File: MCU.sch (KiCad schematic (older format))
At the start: 37 parts, among them SW1 SW_Push, U1 STM32F407IGTx, Y1 12MHz, 20pF

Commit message: small revisions
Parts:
- added F?: 500mA, symbol Device:Fuse
- added J?: USB_B_Mini, symbol Connector:USB_B_Mini
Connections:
- net GND: now also J?.5 (GND), J?.6 (Shield)
- new net: F?.2, J?.1 (VBUS)
- new net 5V_USB: F?.1
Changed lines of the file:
@@
 U 1 1 5FAB40A6
 P 5500 1350
-F 0 "R2" V 5295 1350 50  0000 C CNN
-F 1 "1k" V 5386 1350 50  0000 C CNN
+F 0 "R2" V 5450 1250 50  0000 C CNN
+F 1 "1k" V 5450 1450 50  0000 C CNN
 F 2 "" H 5500 1350 50  0001 C CNN
 F 3 "~" H 5500 1350 50  0001 C CNN
@@
 U 1 1 5FAECA97
 P 6050 2150
-F 0 "R4" V 5845 2150 50  0000 C CNN
-F 1 "1k" V 5936 2150 50  0000 C CNN
+F 0 "R4" V 6100 2250 50  0000 C CNN
+F 1 "1k" V 6100 2050 50  0000 C CNN
 F 2 "" H 6050 2150 50  0001 C CNN
 F 3 "~" H 6050 2150 50  0001 C CNN
@@
 U 1 1 5FAF53A2
 P 6050 1750
-F 0 "R3" V 5845 1750 50  0000 C CNN
-F 1 "10k" V 5936 1750 50  0000 C CNN
+F 0 "R3" V 6000 1650 50  0000 C CNN
+F 1 "10k" V 6000 1850 50  0000 C CNN
 F 2 "" H 6050 1750 50  0001 C CNN
 F 3 "~" H 6050 1750 50  0001 C CNN
@@
 	12700 2400 12700 2600
 Connection ~ 12700 2600
+$Comp
+L Connector:USB_B_Mini J?
+U 1 1 5FA69DAF
+P 1750 2850
+F 0 "J?" H 1807 3317 50  0000 C CNN
+F 1 "USB_B_Mini" H 1807 3226 50  0000 C CNN
+F 2 "" H 1900 2800 50  0001 C CNN
+F 3 "~" H 1900 2800 50  0001 C CNN
+	1    1750 2850
+	1    0    0    -1
+$EndComp
+Text GLabel 2550 2400 1    50   Input ~ 0
+5V_USB
+$Comp
+L Device:Fuse F?
+U 1 1 5FA6B443
+P 2300 2650
+F 0 "F?" V 2103 2650 50  0000 C CNN
+F 1 "500mA" V 2194 2650 50  0000 C CNN
+F 2 "" V 2230 2650 50  0001 C CNN
+F 3 "~" H 2300 2650 50  0001 C CNN
+	1    2300 2650
+	0    1    1    0
+$EndComp
+Wire Wire Line
+	2550 2400 2550 2650
+Wire Wire Line
+	2550 2650 2450 2650
+Wire Wire Line
+	2150 2650 2050 2650
+Wire Wire Line
+	1750 3250 1750 3400
+Wire Wire Line
+	1750 3400 1650 3400
+Wire Wire Line
+	1650 3400 1650 3250
+$Comp
+L power:GND #PWR?
+U 1 1 5FA8CDC1
+P 1650 3550
+F 0 "#PWR?" H 1650 3300 50  0001 C CNN
+F 1 "GND" H 1655 3377 50  0000 C CNN
+F 2 "" H 1650 3550 50  0001 C CNN
+F 3 "" H 1650 3550 50  0001 C CNN
+	1    1650 3550
+	1    0    0    -1
+$EndComp
+Wire Wire Line
+	1650 3550 1650 3400
+Connection ~ 1650 3400
 $EndSCHEMATC

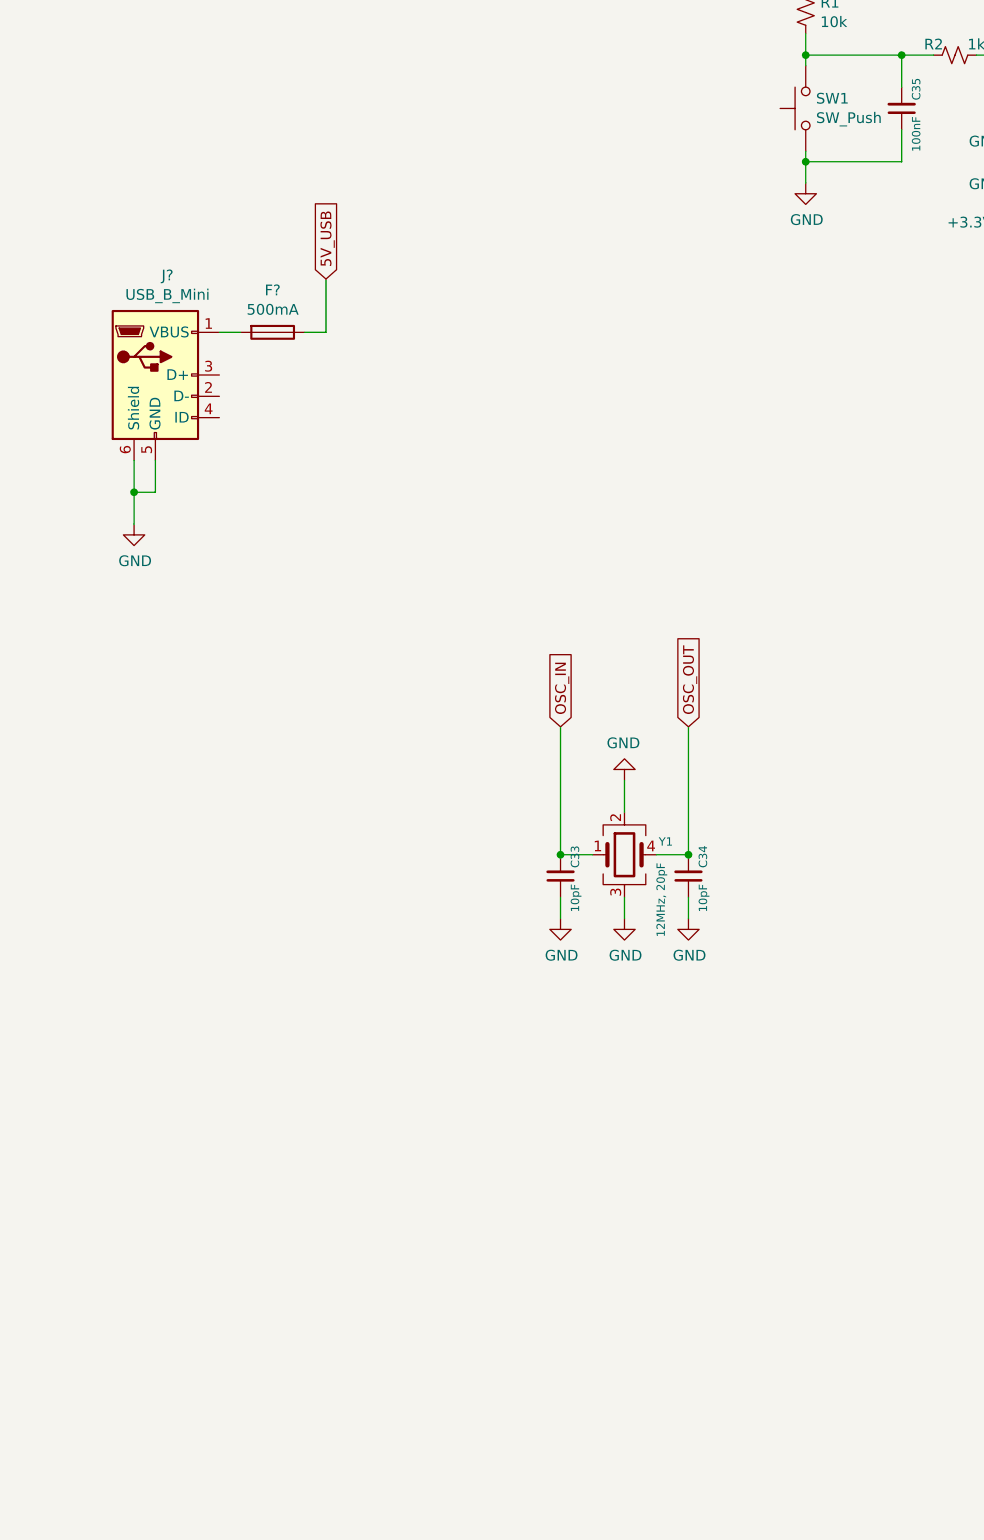
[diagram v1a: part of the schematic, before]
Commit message: added USB and micro SD card
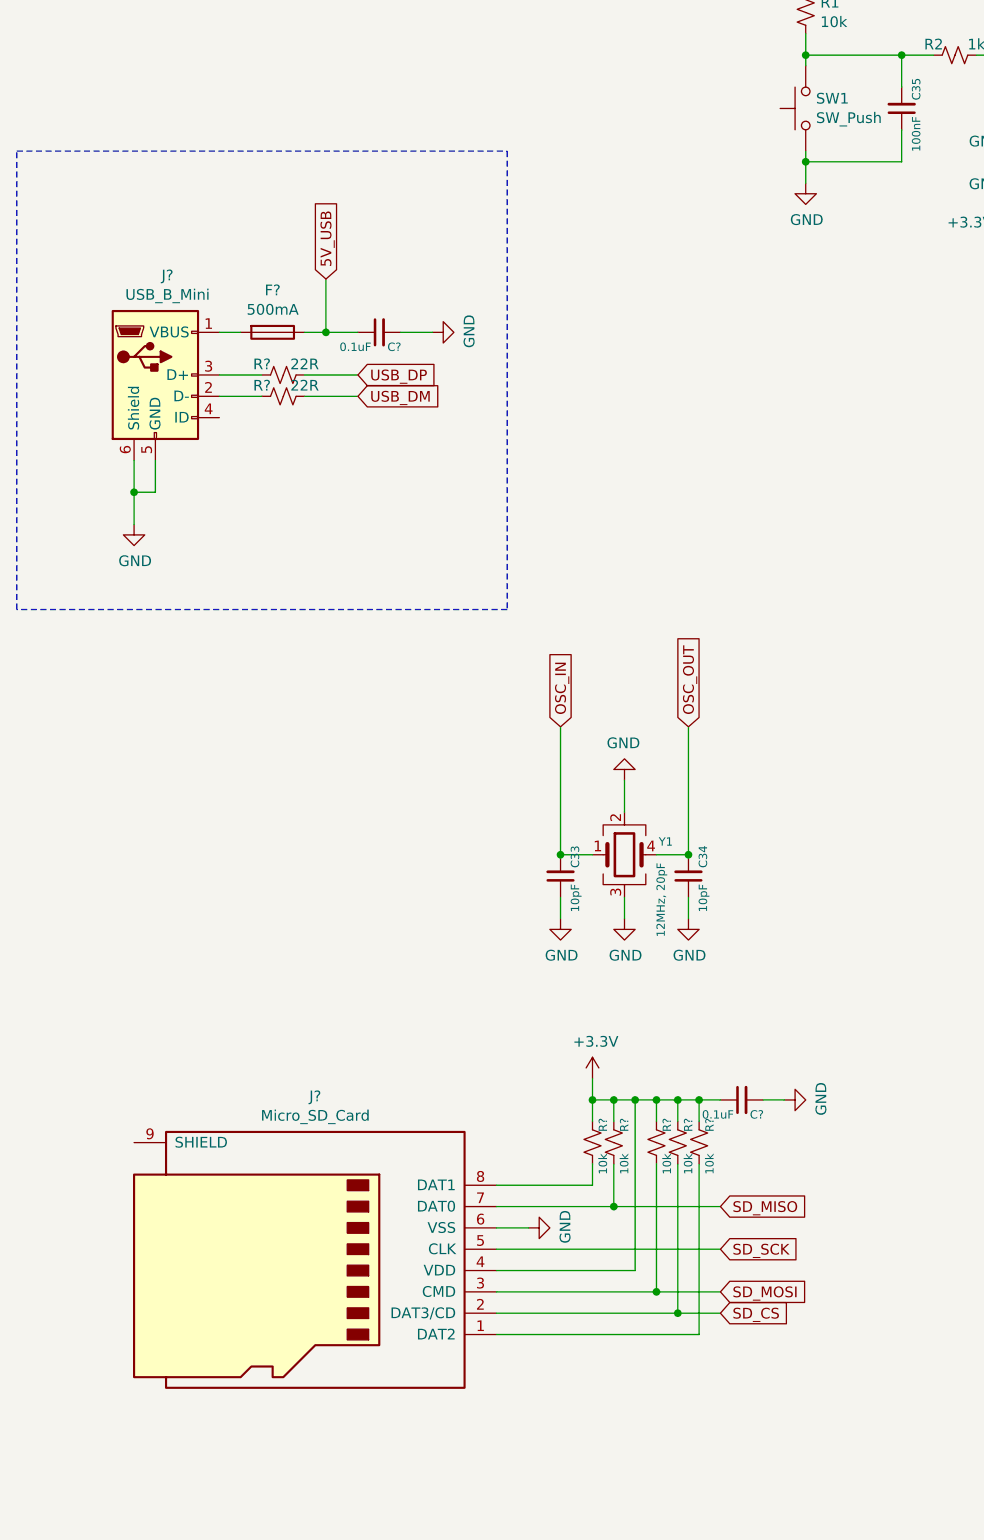
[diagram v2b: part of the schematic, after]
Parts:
- added C? (x2): 0.1uF, symbol Device:C_Small
- added J?: Micro_SD_Card, symbol Connector:Micro_SD_Card
- added R? (x2): 22R, symbol Device:R_Small_US
- added R? (x5): 10k, symbol Device:R_Small_US
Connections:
- net +3V3: now also C?.1, J?.4 (VDD), R?.1, R?.1, R?.1, R?.1, R?.1
- net 5V_USB: now also C?.1
- net GND: now also C?.2, C?.2, J?.6 (VSS)
- net at J?.2 (D-): now also R?.2
- net at J?.3 (D+): now also R?.2
- new net: J?.1 (DAT2), R?.2
- new net: J?.8 (DAT1), R?.2
- new net SD_CS: J?.2 (DAT3/CD), R?.2
- new net SD_MISO: J?.7 (DAT0), R?.2
- new net SD_MOSI: J?.3 (CMD), R?.2
- new net SD_SCK: J?.5 (CLK)
- new net USB_DM: R?.1
- new net USB_DP: R?.1

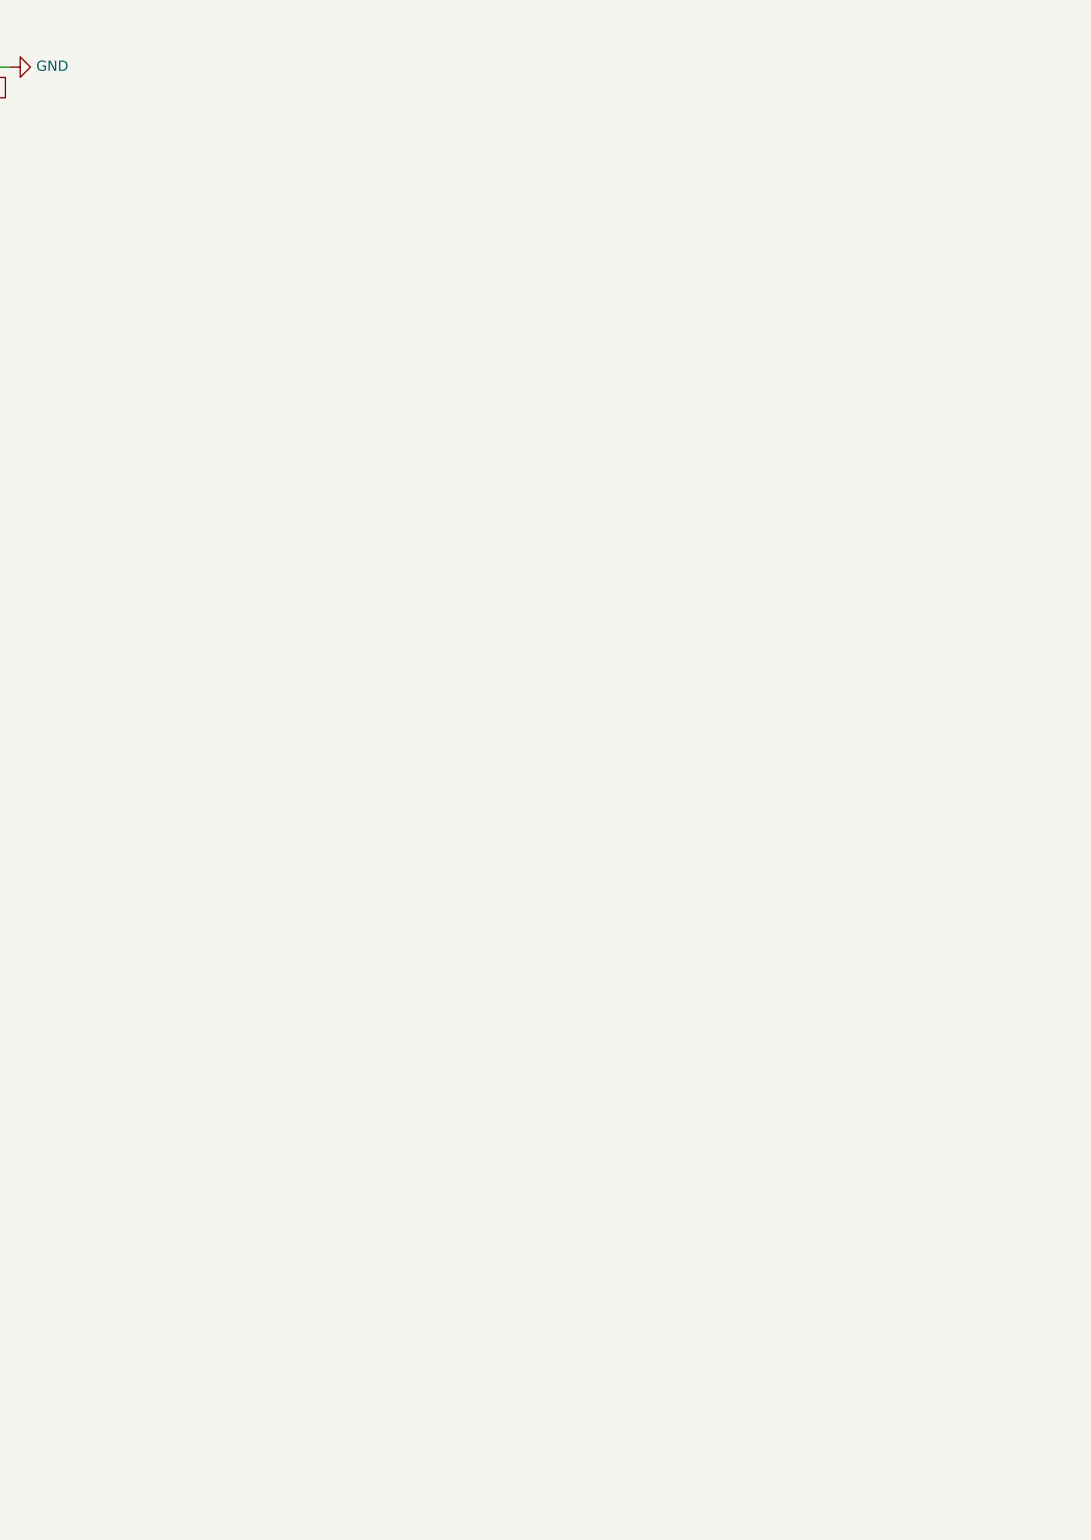
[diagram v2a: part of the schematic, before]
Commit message: added EEPROM and peripheral libraries
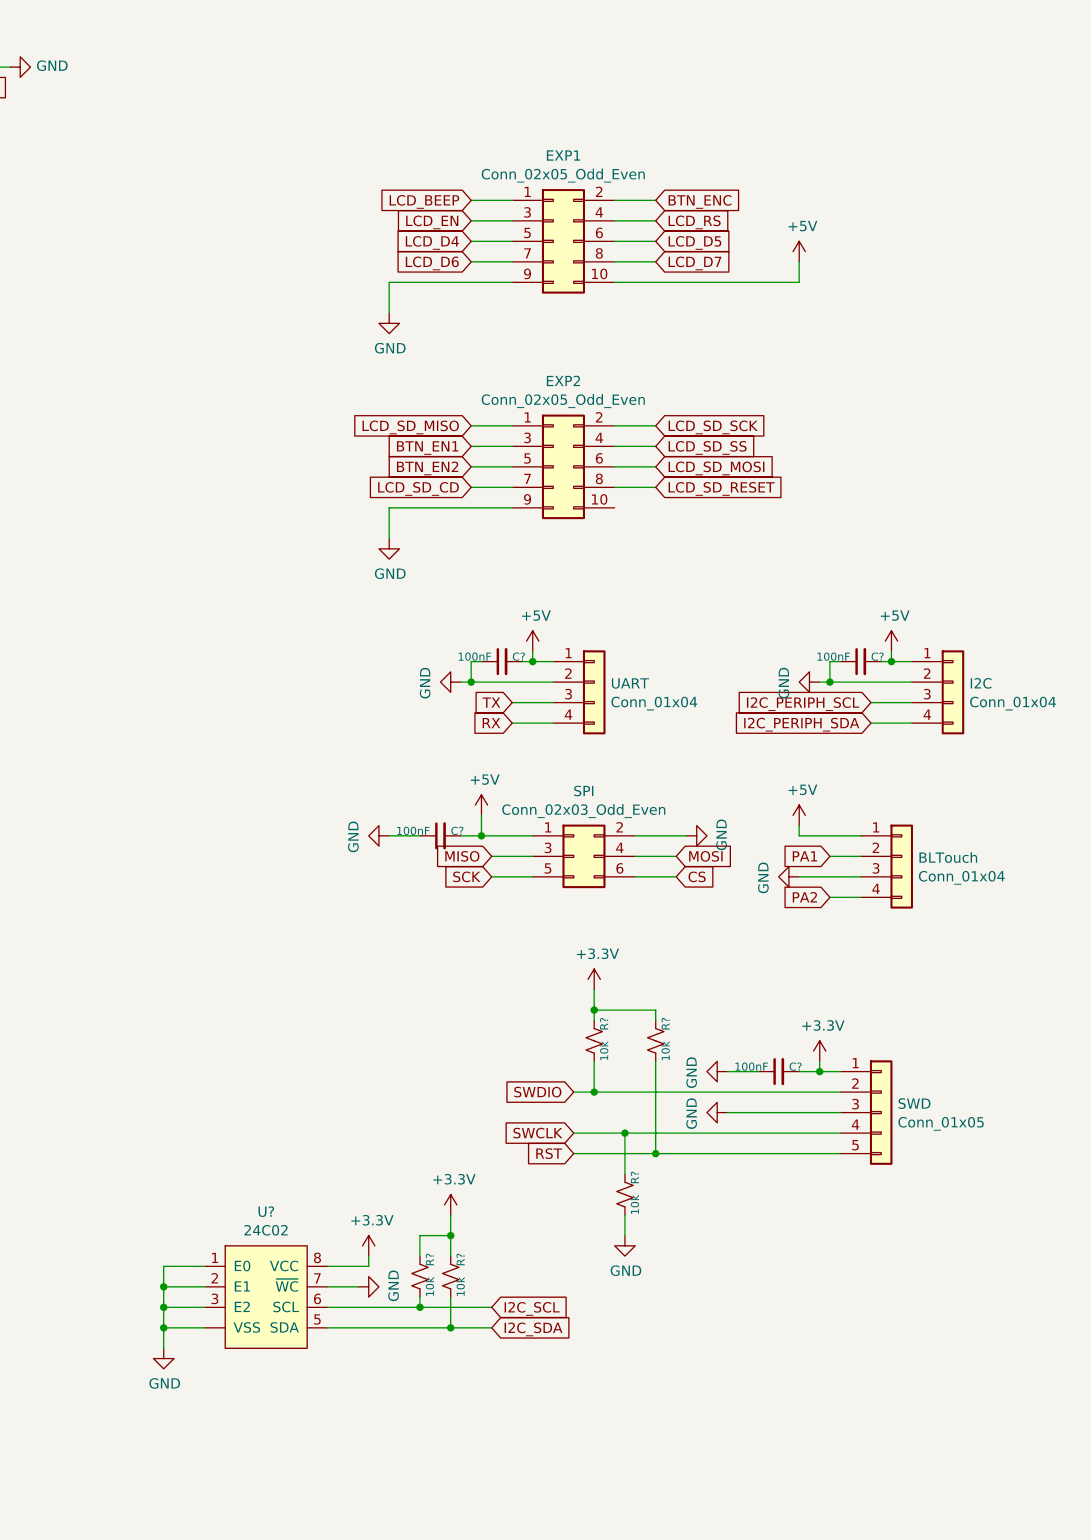
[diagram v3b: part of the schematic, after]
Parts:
- added BLTouch, I2C, UART: Conn_01x04, symbol Connector_Generic:Conn_01x04
- added C? (x4): 100nF, symbol Device:C_Small
- added EXP1, EXP2: Conn_02x05_Odd_Even, symbol Connector_Generic:Conn_02x05_Odd_Even
- added R? (x5): 10k, symbol Device:R_Small_US
- added SPI: Conn_02x03_Odd_Even, symbol Connector_Generic:Conn_02x03_Odd_Even
- added SWD: Conn_01x05, symbol Connector_Generic:Conn_01x05
- added U?: 24C02, symbol EEPROM:24C02
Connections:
- net +3V3: now also C?.2, R?.1, R?.1, R?.1, R?.1, SWD.1 (Pin_1), U?.8 (VCC)
- net GND: now also BLTouch.3 (Pin_3), C?.1, C?.1, C?.1, C?.1, EXP1.9 (Pin_9), EXP2.9 (Pin_9), I2C.2 (Pin_2), R?.2, SPI.2 (Pin_2), SWD.3 (Pin_3), U?.1 (E0), U?.2 (E1), U?.3 (E2), U?.7 (~WC), U?.~ (VSS), UART.2 (Pin_2)
- new net +5V: BLTouch.1 (Pin_1), C?.2, C?.2, C?.2, EXP1.10 (Pin_10), I2C.1 (Pin_1), SPI.1 (Pin_1), UART.1 (Pin_1)
- new net BTN_EN1: EXP2.3 (Pin_3)
- new net BTN_EN2: EXP2.5 (Pin_5)
- new net BTN_ENC: EXP1.2 (Pin_2)
- new net CS: SPI.6 (Pin_6)
- new net I2C_PERIPH_SCL: I2C.3 (Pin_3)
- new net I2C_PERIPH_SDA: I2C.4 (Pin_4)
- new net I2C_SCL: R?.2, U?.6 (SCL)
- new net I2C_SDA: R?.2, U?.5 (SDA)
- new net LCD_BEEP: EXP1.1 (Pin_1)
- new net LCD_D4: EXP1.5 (Pin_5)
- new net LCD_D5: EXP1.6 (Pin_6)
- new net LCD_D6: EXP1.7 (Pin_7)
- new net LCD_D7: EXP1.8 (Pin_8)
- new net LCD_EN: EXP1.3 (Pin_3)
- new net LCD_RS: EXP1.4 (Pin_4)
- new net LCD_SD_CD: EXP2.7 (Pin_7)
- new net LCD_SD_MISO: EXP2.1 (Pin_1)
- new net LCD_SD_MOSI: EXP2.6 (Pin_6)
- new net LCD_SD_RESET: EXP2.8 (Pin_8)
- new net LCD_SD_SCK: EXP2.2 (Pin_2)
- new net LCD_SD_SS: EXP2.4 (Pin_4)
- new net MISO: SPI.3 (Pin_3)
- new net MOSI: SPI.4 (Pin_4)
- new net PA1: BLTouch.2 (Pin_2)
- new net PA2: BLTouch.4 (Pin_4)
- new net RST: R?.2, SWD.5 (Pin_5)
- new net RX: UART.4 (Pin_4)
- new net SCK: SPI.5 (Pin_5)
- new net SWCLK: R?.1, SWD.4 (Pin_4)
- new net SWDIO: R?.2, SWD.2 (Pin_2)
- new net TX: UART.3 (Pin_3)

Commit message: Completed Labelling of Schematic - All nets attached
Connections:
- net labels added: BED_HEATER, BED_THERM, CHAMBER_HEATER, CHAMBER_THERM, E0_DIR, E0_EN, E0_STEP, E0_STOP, E0_UART, E1_DIR, E1_EN, E1_STEP, E1_STOP, E1_UART, E2_DIR, E2_EN, E2_STEP, E2_STOP, E2_UART, E3_DIR, E3_EN, E3_STEP, E3_STOP, E3_UART, E4_DIR, E4_EN, E4_STEP, E4_STOP, E4_UART, E5_DIR, E5_EN, E5_STEP, E5_STOP, E5_UART, FAN0, FAN1, FAN2, FAN3, FAN4, FAN5, FAN6, FAN7, HEATER0, HEATER1, HEATER2, HEATER3, HEATER4, HEATER5, PB11, PH11, THERM0, THERM1, THERM2, THERM3, THERM4, THERM5, X_DIR, X_EN, X_STEP, X_STOP, X_UART, Y_DIR, Y_EN, Y_STEP, Y_STOP, Y_UART, Z_DIR, Z_EN, Z_STEP, Z_STOP, Z_UART
- net labels removed: LCD_SD_RESET, PA1, PA2
- wire segments 327 -> 465
